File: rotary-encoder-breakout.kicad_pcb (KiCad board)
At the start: 2 copper layers, 20.4 x 25.5 mm, 3 parts, among them P4 CONN_01X02, P5 CONN_01X03

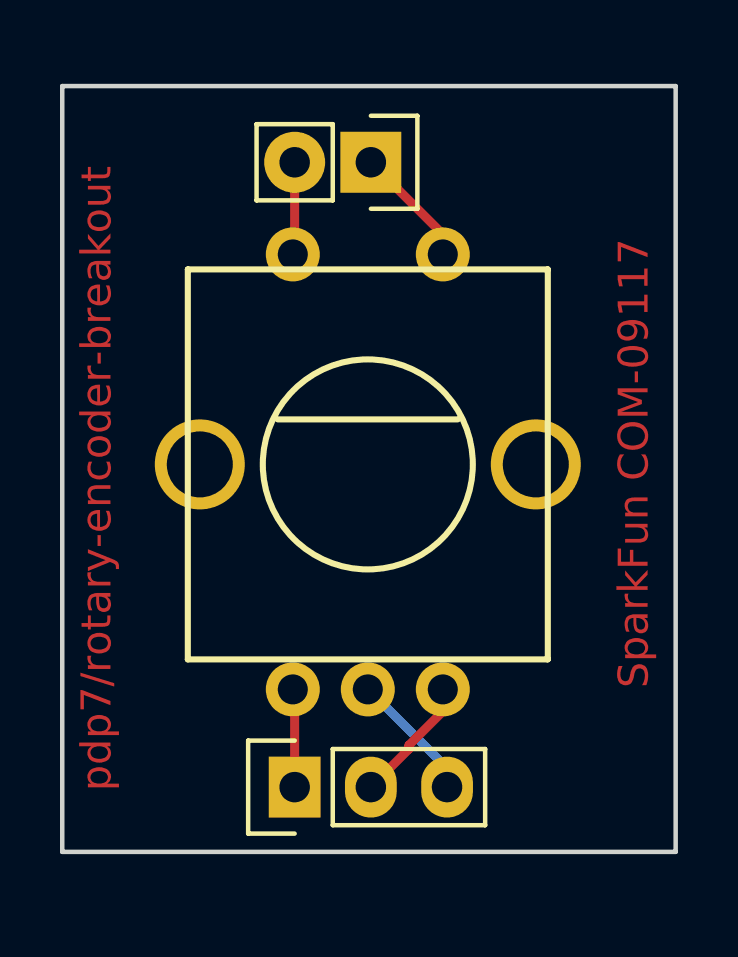
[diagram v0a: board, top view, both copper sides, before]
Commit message: Fix schematic and layout so traces are straight to header
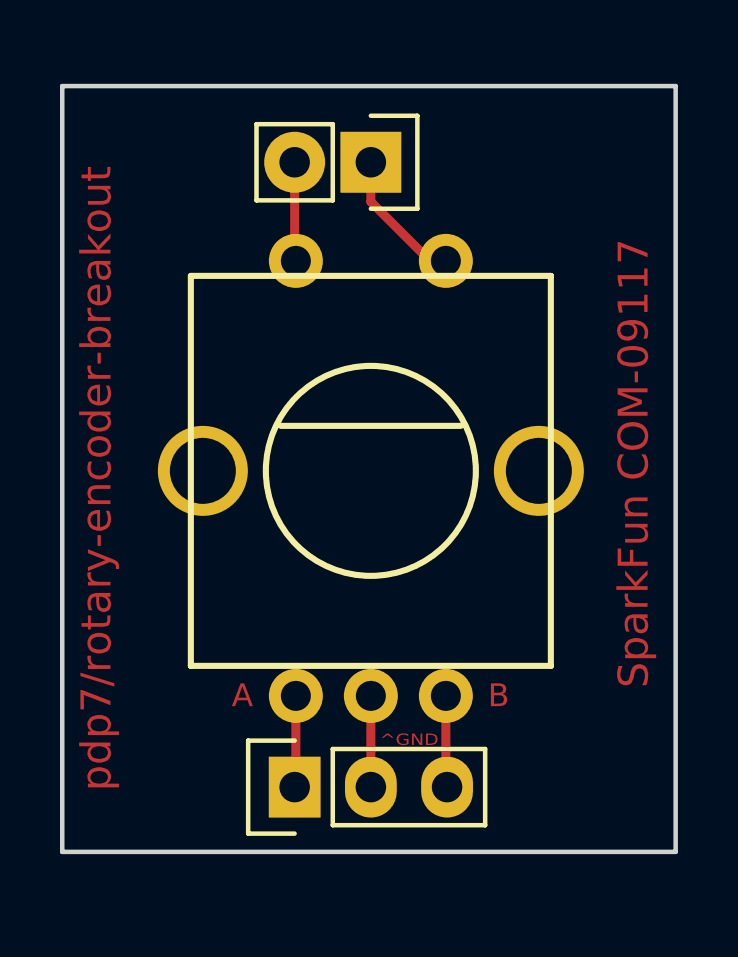
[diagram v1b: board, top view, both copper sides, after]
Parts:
- moved ROT1 0.24 mm to (190.0, 104.1)
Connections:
- ROT1 pad 3: Net-(P5-Pad3) -> Net-(P5-Pad2)
- ROT1 pad 4: Net-(P5-Pad2) -> Net-(P5-Pad3)
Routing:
- net Net-(P5-Pad2): track 4.35 -> 3.04 mm
- net Net-(P5-Pad3): track 4.46 -> 3.69 mm
- net Net-(P4-Pad1): track 4.07 -> 4.63 mm
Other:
- board text added: "A"
- board text added: "B"
- board text added: "^GND"
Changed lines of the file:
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@@
     (links 5)
     (no_connects 0)
-    (area -364.412 25.552285 235.861 119.714333)
+    (area 179.629999 88.819666 200.227001 119.714333)
     (thickness 1.6)
-    (drawings 10)
-    (tracks 15)
+    (drawings 16)
+    (tracks 11)
     (zones 0)
     (modules 3)
@@
     (uvia_drill 0.1)
     (uvias_allowed no)
-    (uvia_min_size 0.2)
-    (uvia_min_drill 0.1)
+    (uvia_min_size 0)
+    (uvia_min_drill 0)
     (pcb_text_width 0.3)
     (pcb_text_size 1.5 1.5)
@@
     (pad_to_mask_clearance 0.2)
     (aux_axis_origin 0 0)
+    (grid_origin 186.11 112.58)
     (visible_elements FFFEFF7F)
     (pcbplotparams
@@
     (add_net "Net-(P5-Pad3)")
   )
+  (module sparkfun:SF-ROTARY-ENCODER (layer F.Cu)
+    (at 189.992 104.14)
+    (fp_text reference ROT1 (at 0 9.5) (layer F.SilkS) hide
+      (effects (font (size 0.762 0.762) (thickness 0.1524)))
+    )
+    (fp_text value ROTARY-ENCODER (at 0 0) (layer F.SilkS) hide
+      (effects (font (size 0.762 0.762) (thickness 0.1524)))
+    )
+    (fp_line (start 3 -1.5) (end -3 -1.5) (layer F.SilkS) (width 0.2032))
+    (fp_circle (center 0 0) (end 3.5 0) (layer F.SilkS) (width 0.2032))
+    (fp_line (start 6 6.5) (end -6 6.5) (layer F.SilkS) (width 0.2032))
+    (fp_line (start -6 6.5) (end -6 -6.5) (layer F.SilkS) (width 0.2032))
+    (fp_line (start -6 -6.5) (end 6 -6.5) (layer F.SilkS) (width 0.2032))
+    (fp_line (start 6 -6.5) (end 6 6.5) (layer F.SilkS) (width 0.2032))
+    (pad 1 thru_hole circle (at -2.5 -7) (size 1.8 1.8) (drill 1) (layers *.Cu *.Mask F.SilkS)
+      (net 2 "Net-(P4-Pad2)"))
+    (pad 2 thru_hole circle (at -2.5 7.5) (size 1.8 1.8) (drill 1) (layers *.Cu *.Mask F.SilkS)
+      (net 3 "Net-(P5-Pad1)"))
+    (pad 3 thru_hole circle (at 0 7.5) (size 1.8 1.8) (drill 1) (layers *.Cu *.Mask F.SilkS)
+      (net 4 "Net-(P5-Pad2)"))
+    (pad 4 thru_hole circle (at 2.5 7.5) (size 1.8 1.8) (drill 1) (layers *.Cu *.Mask F.SilkS)
+      (net 5 "Net-(P5-Pad3)"))
+    (pad 5 thru_hole circle (at 2.5 -7) (size 1.8 1.8) (drill 1) (layers *.Cu *.Mask F.SilkS)
+      (net 1 "Net-(P4-Pad1)"))
+    (pad "" thru_hole circle (at 5.6 0) (size 3 3) (drill 2.2) (layers *.Cu *.Mask F.SilkS))
+    (pad "" thru_hole circle (at -5.6 0) (size 3 3) (drill 2.2) (layers *.Cu *.Mask F.SilkS))
+  )
   (module Pin_Headers:Pin_Header_Straight_1x02 (layer F.Cu)
     (at 189.992 93.853 270)
@@
     )
   )
-  (module sparkfun:SF-ROTARY-ENCODER (layer F.Cu)
-    (at 189.8904 103.9241)
-    (fp_text reference ROT1 (at 0 9.5) (layer F.SilkS) hide
-      (effects (font (size 0.762 0.762) (thickness 0.1524)))
-    )
-    (fp_text value ROTARY-ENCODER (at 0 0) (layer F.SilkS) hide
-      (effects (font (size 0.762 0.762) (thickness 0.1524)))
-    )
-    (fp_line (start 3 -1.5) (end -3 -1.5) (layer F.SilkS) (width 0.2032))
-    (fp_circle (center 0 0) (end 3.5 0) (layer F.SilkS) (width 0.2032))
-    (fp_line (start 6 6.5) (end -6 6.5) (layer F.SilkS) (width 0.2032))
-    (fp_line (start -6 6.5) (end -6 -6.5) (layer F.SilkS) (width 0.2032))
-    (fp_line (start -6 -6.5) (end 6 -6.5) (layer F.SilkS) (width 0.2032))
-    (fp_line (start 6 -6.5) (end 6 6.5) (layer F.SilkS) (width 0.2032))
-    (pad 1 thru_hole circle (at -2.5 -7) (size 1.8 1.8) (drill 1) (layers *.Cu *.Mask F.SilkS)
-      (net 2 "Net-(P4-Pad2)"))
-    (pad 2 thru_hole circle (at -2.5 7.5) (size 1.8 1.8) (drill 1) (layers *.Cu *.Mask F.SilkS)
-      (net 3 "Net-(P5-Pad1)"))
-    (pad 3 thru_hole circle (at 0 7.5) (size 1.8 1.8) (drill 1) (layers *.Cu *.Mask F.SilkS)
-      (net 5 "Net-(P5-Pad3)"))
-    (pad 4 thru_hole circle (at 2.5 7.5) (size 1.8 1.8) (drill 1) (layers *.Cu *.Mask F.SilkS)
-      (net 4 "Net-(P5-Pad2)"))
-    (pad 5 thru_hole circle (at 2.5 -7) (size 1.8 1.8) (drill 1) (layers *.Cu *.Mask F.SilkS)
-      (net 1 "Net-(P4-Pad1)"))
-    (pad "" thru_hole circle (at 5.6 0) (size 3 3) (drill 2.2) (layers *.Cu *.Mask F.SilkS))
-    (pad "" thru_hole circle (at -5.6 0) (size 3 3) (drill 2.2) (layers *.Cu *.Mask F.SilkS))
+  (gr_text ^GND (at 191.27 113.1) (layer F.Mask)
+    (effects (font (size 0.381 0.4572) (thickness 0.0762)))
+  )
+  (gr_text ^GND (at 191.27 113.1) (layer F.Cu)
+    (effects (font (size 0.381 0.4572) (thickness 0.0762)))
+  )
+  (gr_text B (at 194.25 111.63) (layer F.Cu)
+    (effects (font (size 0.762 0.762) (thickness 0.127)))
+  )
+  (gr_text B (at 194.25 111.63) (layer F.Mask)
+    (effects (font (size 0.762 0.762) (thickness 0.127)))
+  )
+  (gr_text "A\n" (at 185.71 111.63) (layer F.Mask)
+    (effects (font (size 0.762 0.762) (thickness 0.127)))
+  )
+  (gr_text "A\n" (at 185.71 111.63) (layer F.Cu)
+    (effects (font (size 0.762 0.762) (thickness 0.127)))
   )
   (gr_text "https://github.com/pdp7\nrotary-encoder-breakout\n" (at 189.992 99.822) (layer B.SilkS)
@@
     (effects (font (size 1 1) (thickness 0.15)))
   )
-  (segment (start 189.992 93.853) (end 192.405 96.266) (width 0.3) (layer F.Cu) (net 1) (status 80000))
-  (segment (start 192.405 96.266) (end 192.405 96.901) (width 0.3) (layer F.Cu) (net 1) (status 80000))
-  (segment (start 192.405 96.901) (end 192.3904 96.9241) (width 0.3) (layer F.Cu) (net 1) (status 80000))
-  (segment (start 187.452 93.853) (end 187.452 96.901) (width 0.3) (layer F.Cu) (net 2) (status 80000))
-  (segment (start 187.452 96.901) (end 187.3904 96.9241) (width 0.3) (layer F.Cu) (net 2) (status 80000))
-  (segment (start 187.452 114.681) (end 187.452 111.379) (width 0.3) (layer F.Cu) (net 3) (status 80000))
-  (segment (start 187.452 111.379) (end 187.3904 111.4241) (width 0.3) (layer F.Cu) (net 3) (status 80000))
-  (segment (start 189.992 114.681) (end 191.262 113.411) (width 0.3) (layer F.Cu) (net 4) (status 80000))
-  (segment (start 191.262 113.411) (end 191.262 113.284) (width 0.3) (layer F.Cu) (net 4) (status 80000))
-  (segment (start 191.262 113.284) (end 192.405 112.141) (width 0.3) (layer F.Cu) (net 4) (status 80000))
-  (segment (start 192.405 112.141) (end 192.405 111.379) (width 0.3) (layer F.Cu) (net 4) (status 80000))
-  (segment (start 192.405 111.379) (end 192.3904 111.4241) (width 0.3) (layer F.Cu) (net 4) (status 80000))
+  (segment (start 189.992 93.853) (end 189.992 95.169) (width 0.3) (layer F.Cu) (net 1))
+  (segment (start 189.992 95.169) (end 191.963 97.14) (width 0.3) (layer F.Cu) (net 1))
+  (segment (start 191.963 97.14) (end 192.492 97.14) (width 0.3) (layer F.Cu) (net 1))
+  (segment (start 187.452 93.853) (end 187.452 97.1) (width 0.3) (layer F.Cu) (net 2))
+  (segment (start 187.452 97.1) (end 187.492 97.14) (width 0.3) (layer F.Cu) (net 2))
+  (segment (start 187.492 111.64) (end 187.492 114.641) (width 0.3) (layer F.Cu) (net 3))
+  (segment (start 187.492 114.641) (end 187.452 114.681) (width 0.3) (layer F.Cu) (net 3))
+  (segment (start 189.992 111.64) (end 189.992 114.681) (width 0.3) (layer F.Cu) (net 4))
+  (segment (start 192.492 111.64) (end 192.492 114.641) (width 0.3) (layer F.Cu) (net 5))
+  (segment (start 192.492 114.641) (end 192.532 114.681) (width 0.3) (layer F.Cu) (net 5))
   (segment (start 192.532 114.681) (end 192.532 114.046) (width 0.3) (layer B.Cu) (net 5) (status 80000))
-  (segment (start 192.532 114.046) (end 189.865 111.379) (width 0.3) (layer B.Cu) (net 5) (status 80000))
-  (segment (start 189.865 111.379) (end 189.8904 111.4241) (width 0.3) (layer B.Cu) (net 5) (status 80000))
 )

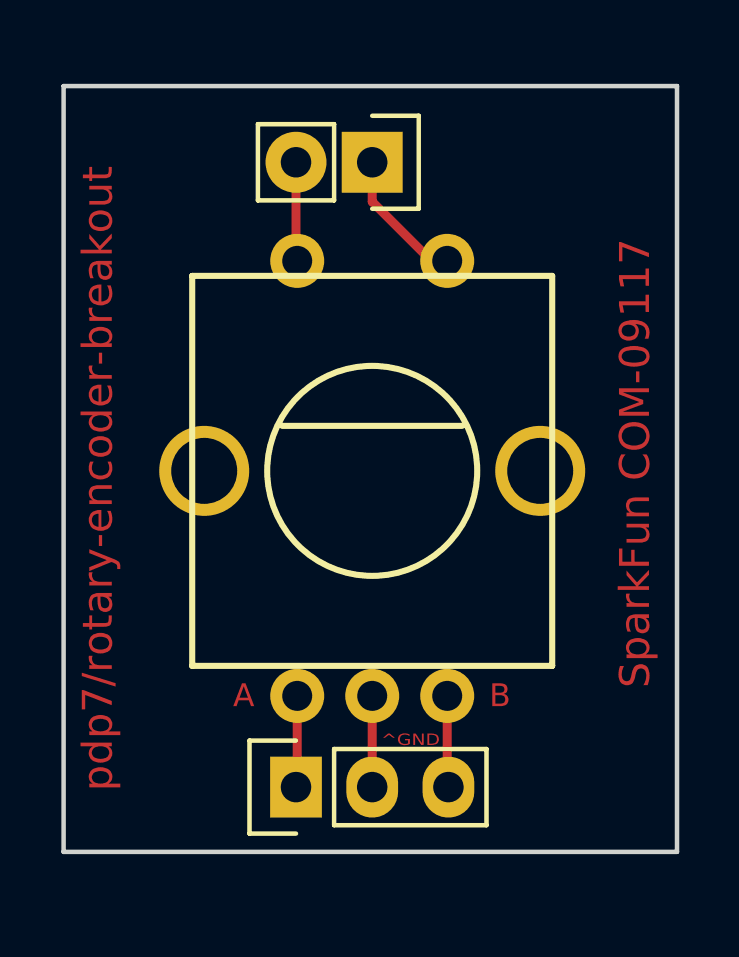
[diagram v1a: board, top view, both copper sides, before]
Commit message: reduce board dimensions to better fit on breadboard
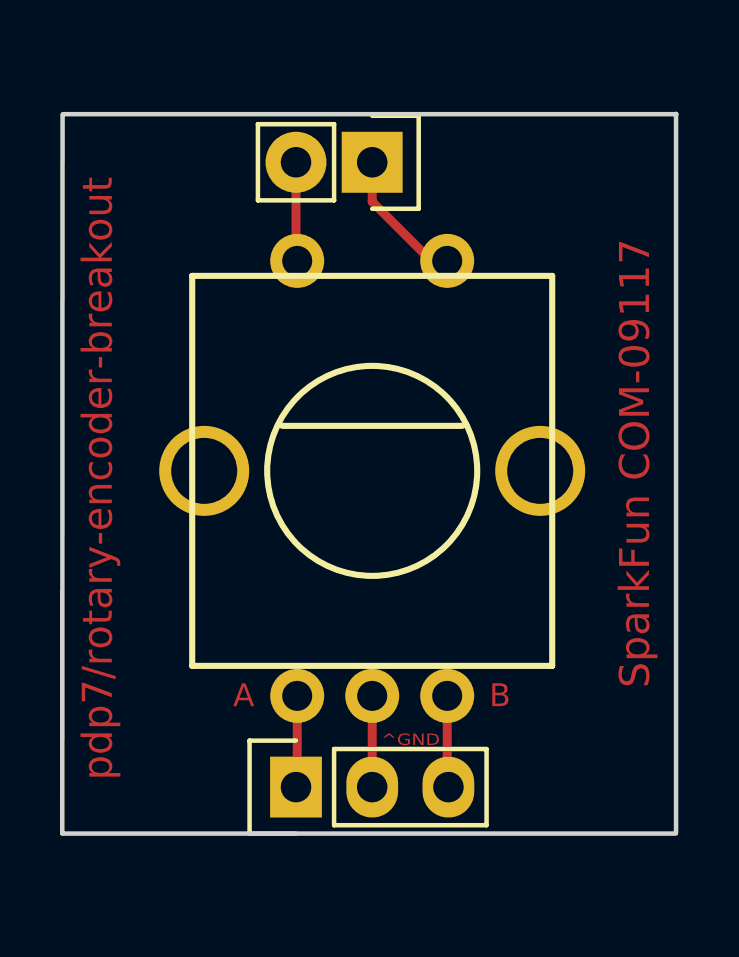
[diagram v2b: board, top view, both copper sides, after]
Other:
- board size 20.4 x 25.5 mm -> 20.5 x 24 mm
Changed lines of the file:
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@@
     (links 5)
     (no_connects 0)
-    (area 179.629999 88.819666 200.227001 119.714333)
+    (area 179.607999 88.819666 200.227001 119.714333)
     (thickness 1.6)
     (drawings 16)
@@
     (effects (font (size 1 1) (thickness 0.15)) (justify mirror))
   )
-  (gr_line (start 179.705 116.84) (end 179.705 91.313) (angle 90) (layer Edge.Cuts) (width 0.15))
-  (gr_line (start 200.152 116.84) (end 179.705 116.84) (angle 90) (layer Edge.Cuts) (width 0.15))
-  (gr_line (start 200.152 91.313) (end 200.152 116.84) (angle 90) (layer Edge.Cuts) (width 0.15))
-  (gr_line (start 179.705 91.313) (end 200.152 91.313) (angle 90) (layer Edge.Cuts) (width 0.15))
+  (gr_line (start 179.66 116.21) (end 179.67 92.27) (angle 90) (layer Edge.Cuts) (width 0.15))
+  (gr_line (start 200.11 116.23) (end 179.663 116.23) (angle 90) (layer Edge.Cuts) (width 0.15))
+  (gr_line (start 200.12 92.24) (end 200.12 116.2) (angle 90) (layer Edge.Cuts) (width 0.15))
+  (gr_line (start 179.683 92.25) (end 200.13 92.25) (angle 90) (layer Edge.Cuts) (width 0.15))
   (gr_text "SparkFun COM-09117\n" (at 198.755 103.886 90) (layer F.Mask)
     (effects (font (size 1 1) (thickness 0.15)))
@@
   )
   (gr_text "pdp7/rotary-encoder-breakout\n" (at 180.848 104.394 90) (layer F.Mask)
-    (effects (font (size 1 1) (thickness 0.15)))
+    (effects (font (size 1 0.9652) (thickness 0.15)))
   )
   (gr_text "pdp7/rotary-encoder-breakout\n" (at 180.848 104.394 90) (layer F.Cu)
-    (effects (font (size 1 1) (thickness 0.15)))
+    (effects (font (size 1 0.9652) (thickness 0.15)))
   )
   (segment (start 189.992 93.853) (end 189.992 95.169) (width 0.3) (layer F.Cu) (net 1))

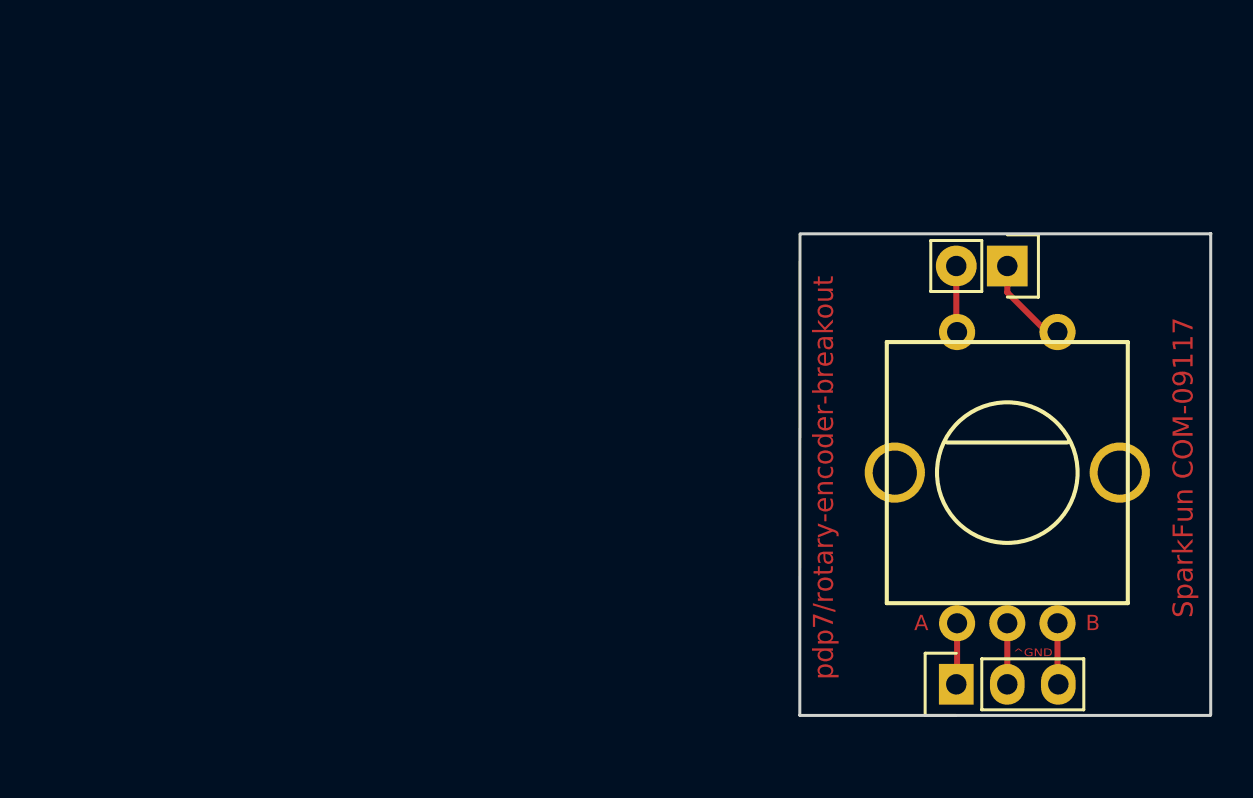
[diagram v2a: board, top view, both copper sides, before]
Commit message: create version with pull-up resistors
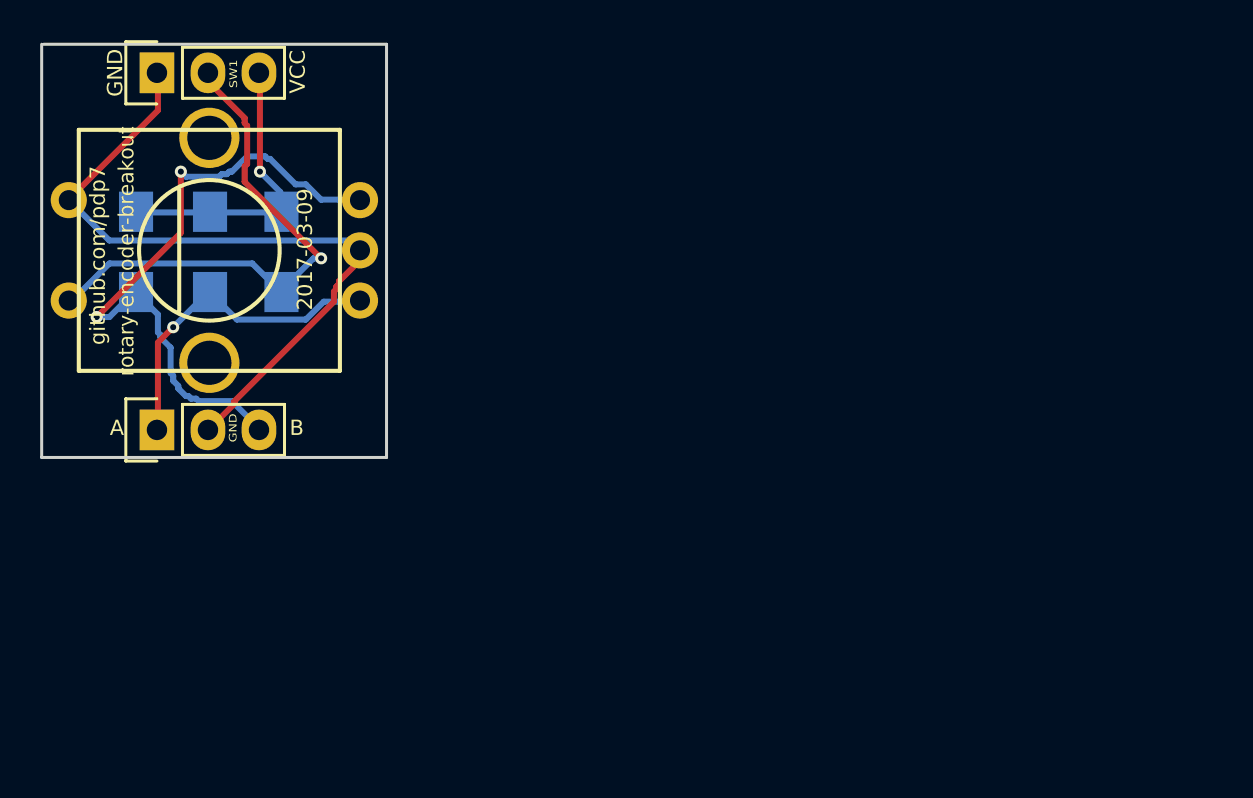
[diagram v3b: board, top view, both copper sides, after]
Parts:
- removed P4: CONN_01X02, Pin_Headers:Pin_Header_Straight_1x02
- added P1: CONN_01X03, Pin_Headers:Pin_Header_Straight_1x03, F.Cu at (147.7, 84.2)
- added R1: R, Resistors_SMD:R_1206_HandSoldering, B.Cu at (146.6, 93.1)
- added R2: R, Resistors_SMD:R_1206_HandSoldering, B.Cu at (150.3, 93.1)
- added R3: R, Resistors_SMD:R_1206_HandSoldering, B.Cu at (153.9, 93.1)
- moved P5 41.8 mm to (147.7, 102.0)
- moved ROT1 41.2 mm to (150.3, 93.1), turned to 90 degrees
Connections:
- P5 pad 2: Net-(P5-Pad2) -> Net-(P1-Pad1)
- ROT1 pad 3: Net-(P5-Pad2) -> Net-(P1-Pad1)
- ROT1 pad 5: Net-(P4-Pad1) -> Net-(P1-Pad1)
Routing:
- net Net-(P1-Pad1): track 0.00 -> 35.9 mm
- net Net-(P5-Pad3): track 3.69 -> 32.6 mm, vias 0 -> 2
- net Net-(P1-Pad2): track 3.30 -> 26.6 mm, vias 0 -> 1
- net /VCC: track 0.00 -> 15.0 mm, vias 0 -> 1
- net Net-(P5-Pad1): track 3.06 -> 16.6 mm, vias 0 -> 1
- net Net-(P4-Pad1): track 4.63 -> 0.00 mm
- net Net-(P5-Pad2): track 3.04 -> 0.00 mm
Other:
- board size 20.5 x 24 mm -> 17.2 x 20.6 mm
- rule trace_min: 0.2 -> 0.2032
- rule via_min_drill: 0.3 -> 0.2794
- rule via_min_size: 0.4 -> 0.381
- board text added: "2017-03-09"
- board text added: "GND"
- board text added: "SW1"
- board text added: "VCC"
- board text added: "github.com/pdp7"
- board text added: "rotary-encoder-breakout"
- board text removed: "SparkFun COM-09117"
- board text removed: "SparkFun COM-09117 318-ENC130175F-12PS"
- board text removed: "^GND"
- board text removed: "https://github.com/pdp7 rotary-encoder-breakout"
- board text removed: "pdp7/rotary-encoder-breakout"
